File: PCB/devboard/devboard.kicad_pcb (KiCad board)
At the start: 2 copper layers, 27 x 43.4 mm, 45 parts, among them J1 Conn_01x13_Pin, J3 Micro_SD_Card, J4 USB_C_Receptacle_USB2.0_14P, SW1 SW_Push, SW2 SW_Push, U1 ESP32-C6, U2 TPS62172DSG, U3 W25Q64JVSSIQ, Y1 C521661, Y3 Crystal

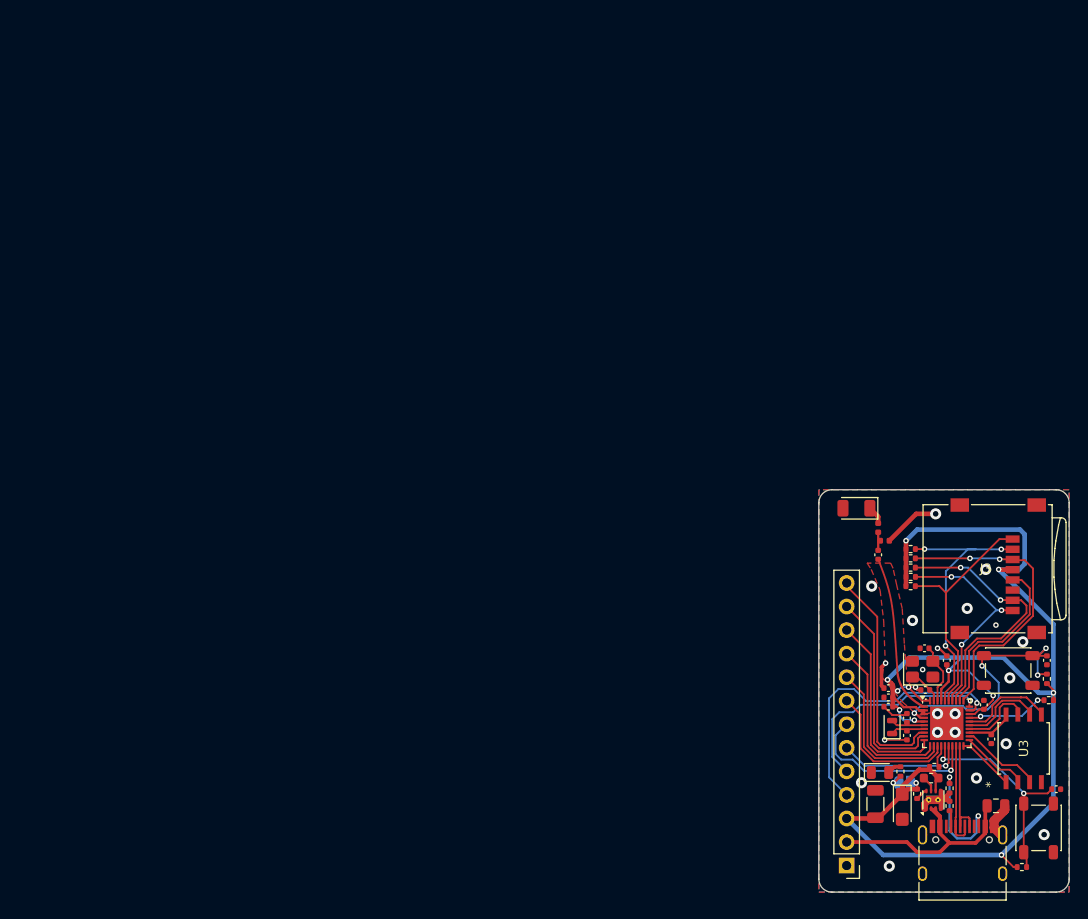
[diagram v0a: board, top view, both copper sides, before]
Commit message: move the pcb to the corner
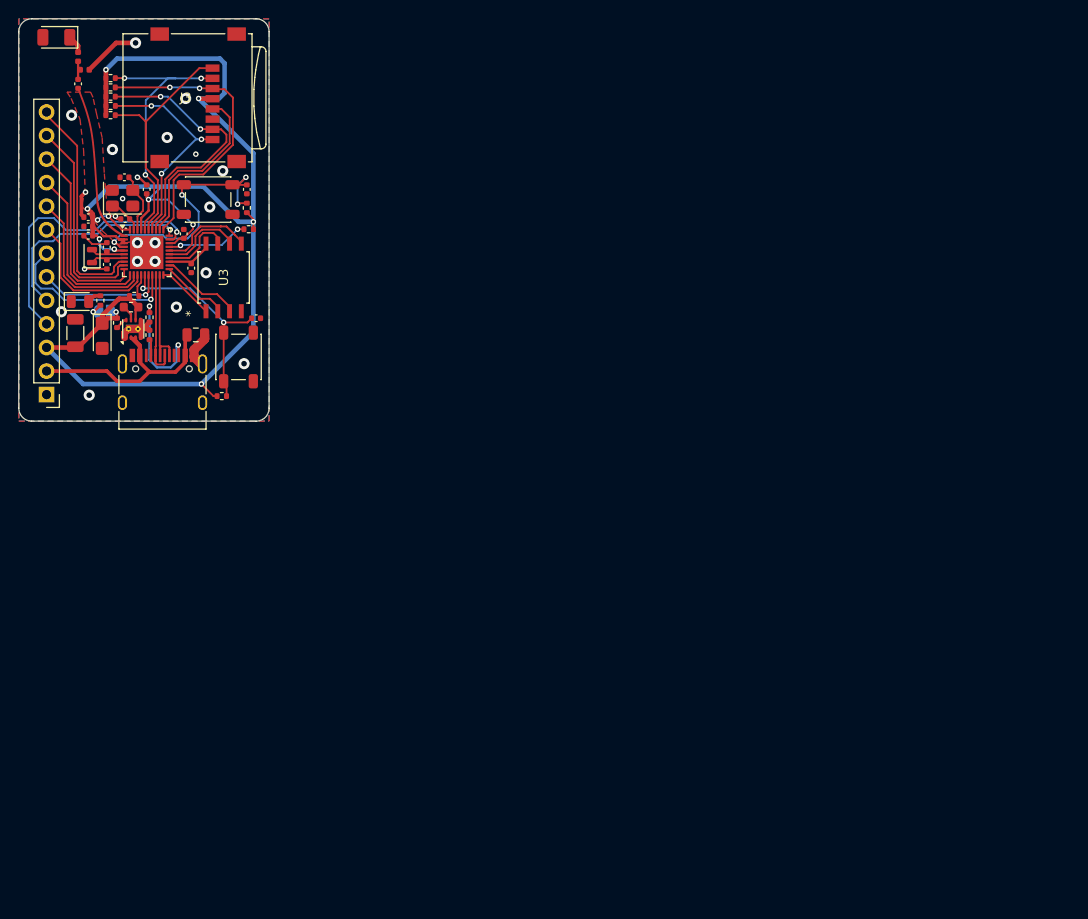
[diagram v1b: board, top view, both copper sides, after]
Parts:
- moved C1 100.1 mm to (36.6, 30.4)
- moved C13 100.1 mm to (18.4, 19.0)
- moved C15 100.1 mm to (30.6, 38.9)
- moved C16 100.1 mm to (37.6, 44.3)
- moved C2 100.1 mm to (23.4, 29.1)
- moved C6 100.1 mm to (31.1, 46.1)
- moved C7 100.1 mm to (18.1, 45.9)
- moved D1 100.1 mm to (18.6, 42.5)
- moved J3 100.1 mm to (31.4, 20.5)
- moved L2 100.1 mm to (18.4, 16.1)
- moved L3 100.1 mm to (19.1, 17.5)
- moved R1 100.1 mm to (33.9, 52.7)
- moved R10 100.1 mm to (21.9, 22.4)
- moved R11 100.1 mm to (21.9, 18.4)
- moved R12 100.1 mm to (21.9, 19.4)
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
